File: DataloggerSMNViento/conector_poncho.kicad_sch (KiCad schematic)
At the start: 1 part

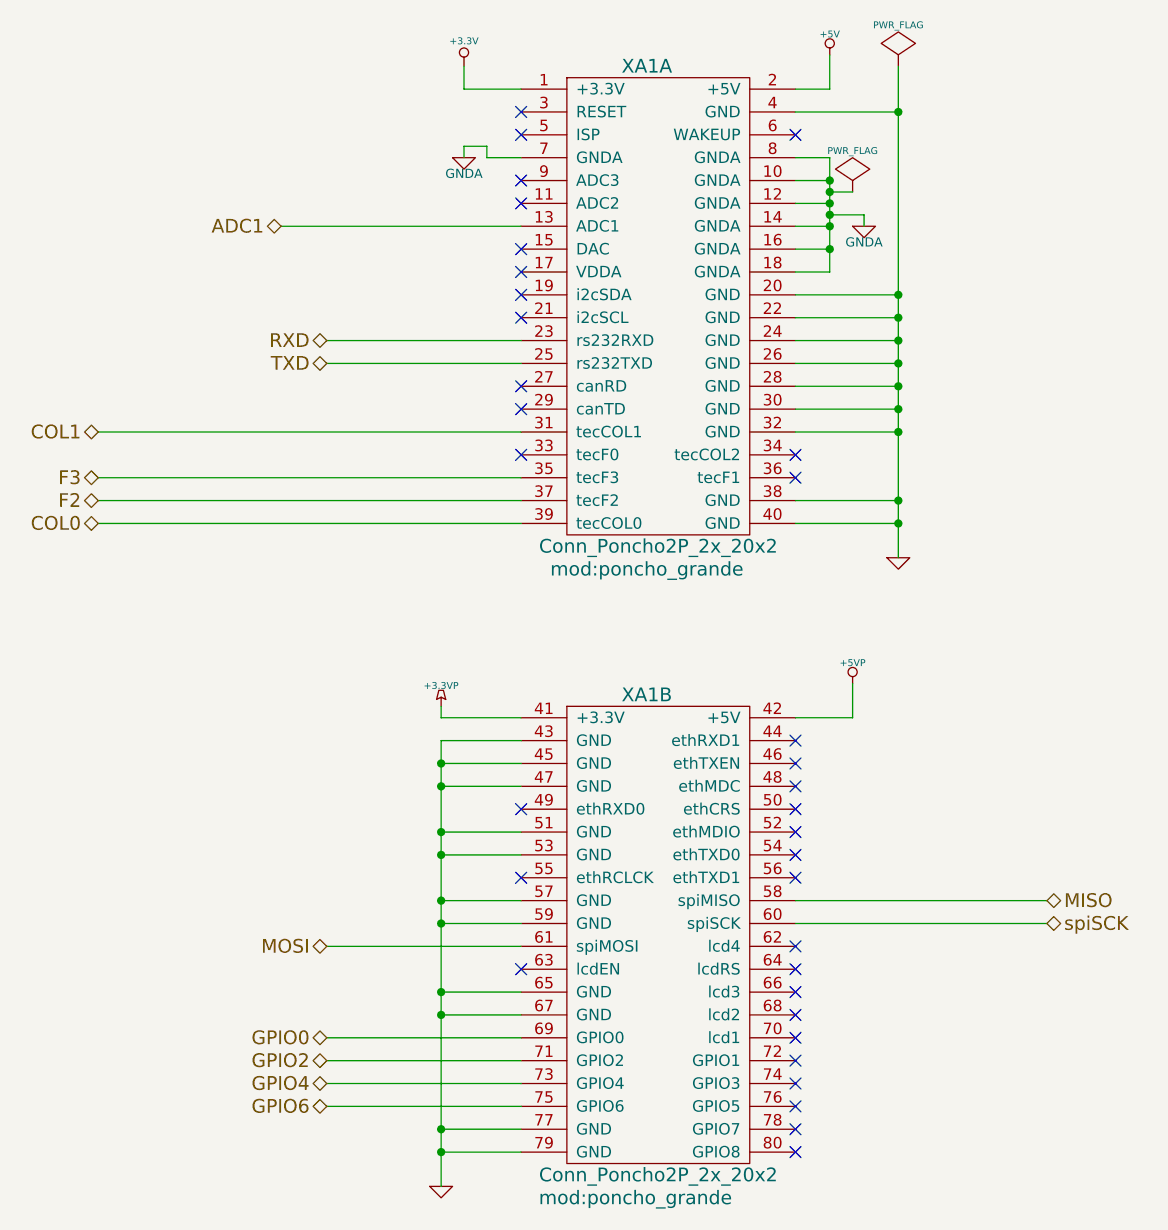
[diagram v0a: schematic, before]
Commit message: Agrego modificaciones al poncho de la EDU CIAA, también agrego una simulacion del circuito para tomar la tensión del ADC del tunnel
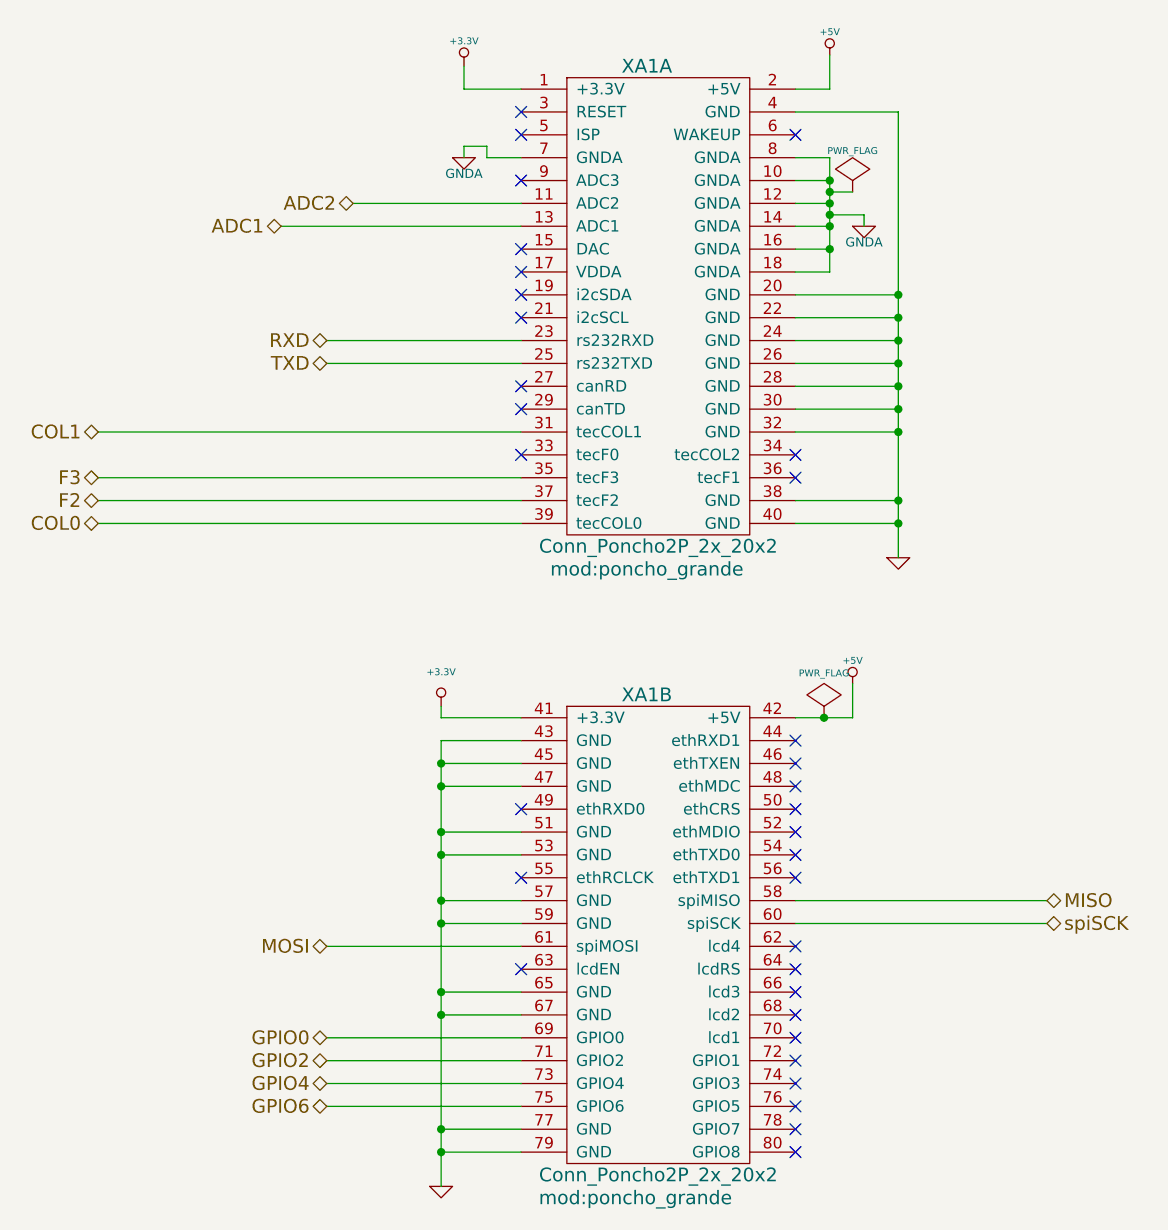
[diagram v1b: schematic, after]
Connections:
- net +3.3VP is gone; now on net +3.3V: XA1.41 (+3.3V)
- net +5VP is gone; now on net +5V: XA1.42 (+5V)
- net ADC2: now reaches XA1.11 (ADC2)
- no-connect marks 34 -> 33
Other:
- company: Compañia: Servicio Meteorologico Nacional - Universidad de Buenos Aires -> Servicio Meteorológico Nacional - FIUBA - UBA
- title: Poncho Grande - Datalogger SMN Viento -> Datalogger para SCTV
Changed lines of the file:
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@@
   (paper "A4")
   (title_block
-    (title "Poncho Grande - Datalogger SMN Viento")
-    (date "2015-10-06")
+    (title "Datalogger para SCTV")
+    (date "2023-10-20")
     (rev "1.0")
-    (company "Compañia: Servicio Meteorologico Nacional - Universidad de Buenos Aires")
-    (comment 1 "https://github.com/ciaa/Ponchos/tree/master/modelos/doc")
-    (comment 2 "Licencia: Ver Licencia.txt UBA")
-    (comment 3 "Autor del poncho: Cristian Zozimo Aranda Cordero. Ver directorio \"doc\"")
-    (comment 4 "CÓDIGO PONCHO:")
+    (company "Servicio Meteorológico Nacional - FIUBA - UBA")
+    (comment 1 "poner repo")
+    (comment 2 "Autores y Licencia del poncho: Cristian Aranda (FIUBA), ver archivo licence.txt")
+    (comment 3 "Autor del poncho: Cristian Zozimo Aranda Cordero.  Ver directorio \"doc\"")
+    (comment 4 "CÓDIGO PONCHO: DT1")
   )
   (junction (at 171.45 66.04) (diameter 0) (color 0 0 0 0)
@@
   (junction (at 171.45 55.88) (diameter 0) (color 0 0 0 0)
   )
-  (junction (at 171.45 33.02) (diameter 0) (color 0 0 0 0)
-  )
   (junction (at 163.83 45.72) (diameter 0) (color 0 0 0 0)
   )
@@
   )
   (junction (at 120.65 133.35) (diameter 0) (color 0 0 0 0)
+  )
+  (junction (at 163.195 100.33) (diameter 0) (color 0 0 0 0)
   )
   (junction (at 120.65 123.19) (diameter 0) (color 0 0 0 0)
@@
   (no_connect (at 160.02 138.43))
   (no_connect (at 160.02 110.49))
-  (no_connect (at 129.54 43.18))
   (no_connect (at 129.54 53.34))
   (no_connect (at 160.02 133.35))
@@
     (stroke (width 0) (type default) (color 0 0 0 0))
   )
+  (wire (pts (xy 163.195 100.33) (xy 160.02 100.33))
+    (stroke (width 0) (type default) (color 0 0 0 0))
+  )
   (wire (pts (xy 163.83 48.26) (xy 163.83 50.8))
     (stroke (width 0) (type default) (color 0 0 0 0))
@@
     (stroke (width 0) (type default) (color 0 0 0 0))
   )
+  (wire (pts (xy 110.871 43.18) (xy 129.54 43.18))
+    (stroke (width 0) (type default) (color 0 0 0 0))
+  )
   (wire (pts (xy 160.02 78.74) (xy 171.45 78.74))
     (stroke (width 0) (type default) (color 0 0 0 0))
@@
     (stroke (width 0) (type default) (color 0 0 0 0))
   )
-  (wire (pts (xy 171.45 27.94) (xy 171.45 33.02))
-    (stroke (width 0) (type default) (color 0 0 0 0))
-  )
   (wire (pts (xy 171.45 63.5) (xy 171.45 66.04))
     (stroke (width 0) (type default) (color 0 0 0 0))
@@
     (stroke (width 0) (type default) (color 0 0 0 0))
   )
-  (wire (pts (xy 163.83 30.48) (xy 160.02 30.48))
-    (stroke (width 0) (type default) (color 0 0 0 0))
-  )
   (wire (pts (xy 120.65 100.33) (xy 120.65 99.06))
     (stroke (width 0) (type default) (color 0 0 0 0))
@@
     (stroke (width 0) (type default) (color 0 0 0 0))
   )
+  (wire (pts (xy 160.02 30.48) (xy 163.83 30.48))
+    (stroke (width 0) (type default) (color 0 0 0 0))
+  )
   (wire (pts (xy 129.54 78.74) (xy 82.55 78.74))
     (stroke (width 0) (type default) (color 0 0 0 0))
@@
     (stroke (width 0) (type default) (color 0 0 0 0))
   )
-  (wire (pts (xy 166.37 100.33) (xy 160.02 100.33))
+  (wire (pts (xy 166.37 100.33) (xy 163.195 100.33))
     (stroke (width 0) (type default) (color 0 0 0 0))
   )
@@
   (hierarchical_label "MISO" (shape bidirectional) (at 187.96 120.65 0)
     (effects (font (size 1.524 1.524)) (justify left))
+  )
+  (hierarchical_label "ADC2" (shape bidirectional) (at 110.871 43.18 180)
+    (effects (font (size 1.524 1.524)) (justify right))
   )
   (hierarchical_label "ADC1" (shape bidirectional) (at 102.87 45.72 180)
@@
     (pin "1")
   )
-  (symbol (lib_id "Misc_Poncho_Grande:+3.3VP") (at 120.65 99.06 0) (unit 1)
-    (in_bom yes) (on_board yes)
-    (property "Reference" "#PWR02" (id 0) (at 121.92 98.298 0)
-      (effects (font (size 0.508 0.508)) hide)
-    )
-    (property "Value" "+3.3VP" (id 1) (at 120.65 96.774 0)
-      (effects (font (size 0.762 0.762)))
-    )
-    (property "Footprint" "" (id 2) (at 120.65 99.06 0)
-      (effects (font (size 1.524 1.524)))
-    )
-    (property "Datasheet" "" (id 3) (at 120.65 99.06 0)
-      (effects (font (size 1.524 1.524)))
-    )
-    (pin "1")
-  )
   (symbol (lib_id "Misc_Poncho_Grande:GNDA") (at 123.19 38.1 0) (unit 1)
     (in_bom yes) (on_board yes)
@@
     (pin "1")
   )
-  (symbol (lib_id "Misc_Poncho_Grande:PWR_FLAG") (at 171.45 27.94 0) (unit 1)
-    (in_bom yes) (on_board yes)
-    (property "Reference" "#FLG02" (id 0) (at 171.45 25.527 0)
-      (effects (font (size 0.762 0.762)) hide)
-    )
-    (property "Value" "PWR_FLAG" (id 1) (at 171.45 23.368 0)
-      (effects (font (size 0.762 0.762)))
-    )
-    (property "Footprint" "" (id 2) (at 171.45 27.94 0)
-      (effects (font (size 1.524 1.524)))
-    )
-    (property "Datasheet" "" (id 3) (at 171.45 27.94 0)
-      (effects (font (size 1.524 1.524)))
-    )
-    (pin "1")
-  )
   (symbol (lib_id "Misc_Poncho_Grande:PWR_FLAG") (at 166.37 41.91 0) (unit 1)
     (in_bom yes) (on_board yes)
@@
     )
     (property "Datasheet" "" (id 3) (at 166.37 41.91 0)
-      (effects (font (size 1.524 1.524)))
-    )
-    (pin "1")
-  )
-  (symbol (lib_id "Misc_Poncho_Grande:+5V") (at 163.83 26.67 0) (unit 1)
-    (in_bom yes) (on_board yes)
-    (property "Reference" "#PWR06" (id 0) (at 163.83 24.384 0)
-      (effects (font (size 0.508 0.508)) hide)
-    )
-    (property "Value" "+5V" (id 1) (at 163.83 24.384 0)
-      (effects (font (size 0.762 0.762)))
-    )
-    (property "Footprint" "" (id 2) (at 163.83 26.67 0)
-      (effects (font (size 1.524 1.524)))
-    )
-    (property "Datasheet" "" (id 3) (at 163.83 26.67 0)
       (effects (font (size 1.524 1.524)))
     )
@@
     (pin "80")
   )
-  (symbol (lib_id "Poncho_Esqueleto:Conn_Poncho2P_2x_20x2") (at 135.89 38.1 0) (unit 1)
+  (symbol (lib_name "Conn_Poncho2P_2x_20x2_1") (lib_id "Poncho_Esqueleto:Conn_Poncho2P_2x_20x2") (at 135.89 38.1 0) (unit 1)
     (in_bom yes) (on_board yes)
     (property "Reference" "XA1" (id 0) (at 143.51 27.94 0)
@@
     (pin "80")
   )
-  (symbol (lib_id "Misc_Poncho_Grande:+5VP") (at 166.37 96.52 0) (unit 1)
-    (in_bom yes) (on_board yes)
-    (property "Reference" "#PWR07" (id 0) (at 166.37 94.234 0)
+  (symbol (lib_id "Misc_Poncho_Grande:+3.3V") (at 120.65 99.06 0) (unit 1)
+    (in_bom yes) (on_board yes) (fields_autoplaced)
+    (property "Reference" "#PWR0104" (id 0) (at 120.65 100.076 0)
+      (effects (font (size 0.762 0.762)) hide)
+    )
+    (property "Value" "+3.3V" (id 1) (at 120.65 95.25 0)
+      (effects (font (size 0.762 0.762)))
+    )
+    (property "Footprint" "" (id 2) (at 120.65 99.06 0)
+      (effects (font (size 1.524 1.524)))
+    )
+    (property "Datasheet" "" (id 3) (at 120.65 99.06 0)
+      (effects (font (size 1.524 1.524)))
+    )
+    (pin "1")
+  )
+  (symbol (lib_id "Misc_Poncho_Grande:+5V") (at 163.83 26.67 0) (unit 1)
+    (in_bom yes) (on_board yes) (fields_autoplaced)
+    (property "Reference" "#PWR0101" (id 0) (at 163.83 24.384 0)
       (effects (font (size 0.508 0.508)) hide)
     )
-    (property "Value" "+5VP" (id 1) (at 166.37 94.234 0)
+    (property "Value" "+5V" (id 1) (at 163.83 24.13 0)
       (effects (font (size 0.762 0.762)))
     )
+    (property "Footprint" "" (id 2) (at 163.83 26.67 0)
+      (effects (font (size 1.524 1.524)))
+    )
+    (property "Datasheet" "" (id 3) (at 163.83 26.67 0)
+      (effects (font (size 1.524 1.524)))
+    )
+    (pin "1")
+  )
+  (symbol (lib_id "Misc_Poncho_Grande:PWR_FLAG") (at 163.195 100.33 0) (unit 1)
+    (in_bom yes) (on_board yes) (fields_autoplaced)
+    (property "Reference" "#FLG0102" (id 0) (at 163.195 97.917 0)
+      (effects (font (size 0.762 0.762)) hide)
+    )
+    (property "Value" "PWR_FLAG" (id 1) (at 163.195 95.377 0)
+      (effects (font (size 0.762 0.762)))
+    )
+    (property "Footprint" "" (id 2) (at 163.195 100.33 0)
+      (effects (font (size 1.524 1.524)))
+    )
+    (property "Datasheet" "" (id 3) (at 163.195 100.33 0)
+      (effects (font (size 1.524 1.524)))
+    )
+    (pin "1")
+  )
+  (symbol (lib_id "Misc_Poncho_Grande:+5V") (at 166.37 96.52 0) (unit 1)
+    (in_bom yes) (on_board yes) (fields_autoplaced)
+    (property "Reference" "#PWR0105" (id 0) (at 166.37 94.234 0)
+      (effects (font (size 0.508 0.508)) hide)
+    )
+    (property "Value" "+5V" (id 1) (at 166.37 93.98 0)
+      (effects (font (size 0.762 0.762)))
+    )

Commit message: Subo la version v1.0 del PCB del poncho de la tesis
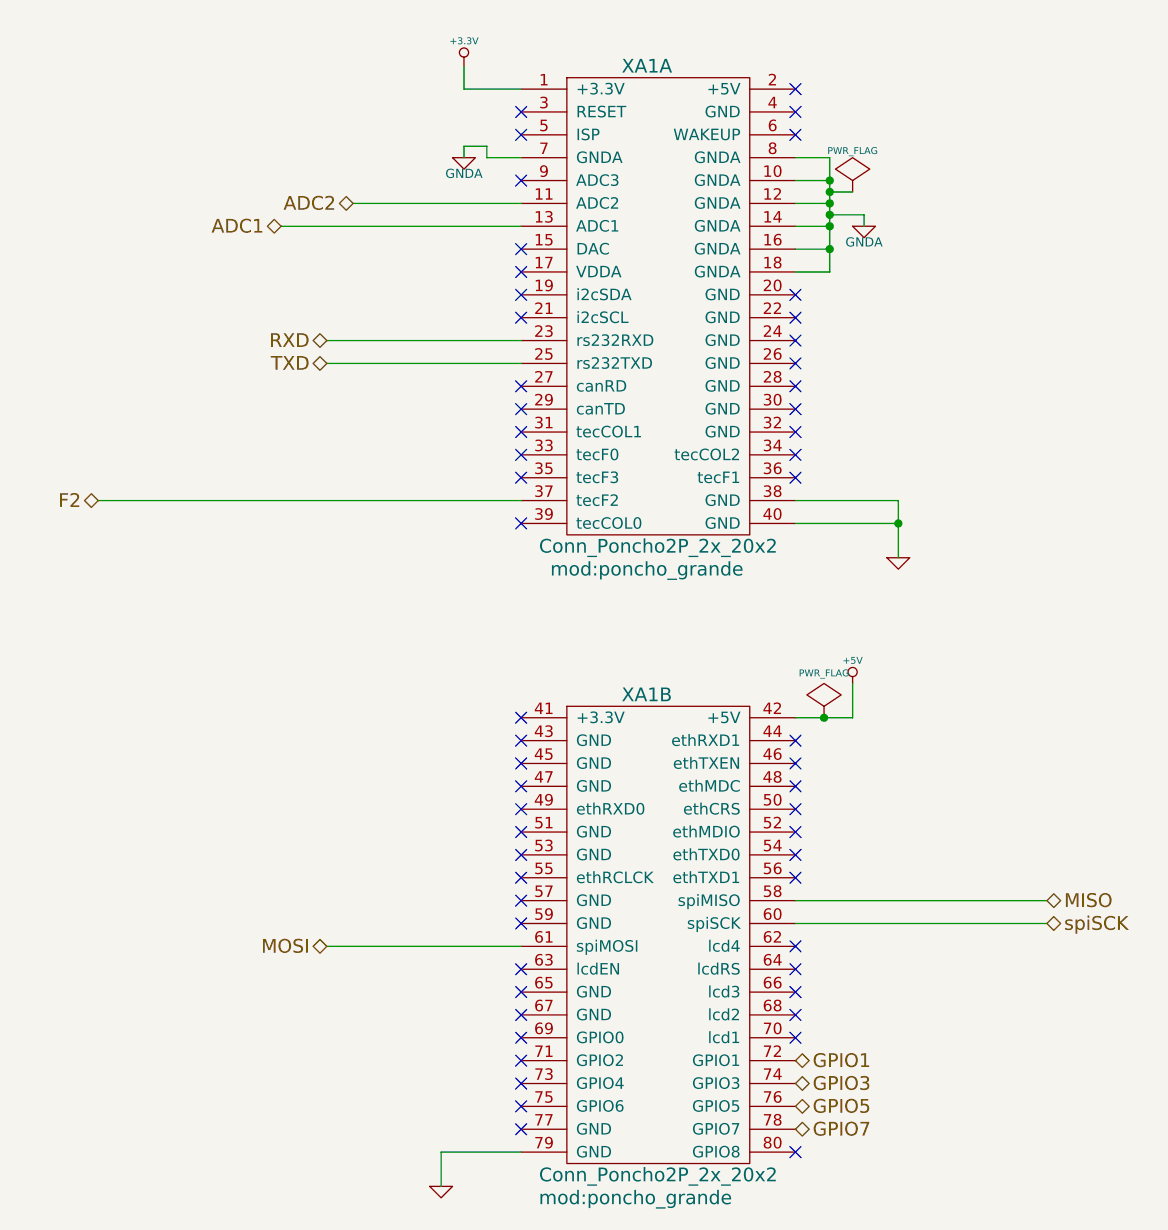
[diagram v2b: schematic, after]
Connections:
- net +3.3V: no longer XA1.41 (+3.3V)
- net +5V: no longer XA1.2 (+5V)
- net GND: no longer XA1.20 (GND), XA1.22 (GND), XA1.24 (GND), XA1.26 (GND), XA1.28 (GND), XA1.30 (GND), XA1.32 (GND), XA1.4 (GND), XA1.43 (GND), XA1.45 (GND), XA1.47 (GND), XA1.51 (GND), XA1.53 (GND), XA1.57 (GND), XA1.59 (GND), XA1.65 (GND), XA1.67 (GND), XA1.77 (GND)
- net GPIO1: now reaches XA1.72 (GPIO1)
- net GPIO3: now reaches XA1.74 (GPIO3)
- net GPIO5: now reaches XA1.76 (GPIO5)
- net GPIO7: now reaches XA1.78 (GPIO7)
- net COL0: no longer names the net of XA1.39 (tecCOL0)
- net COL1: no longer names the net of XA1.31 (tecCOL1)
- net F3: no longer names the net of XA1.35 (tecF3)
- net GPIO0: no longer names the net of XA1.69 (GPIO0)
- net GPIO2: no longer names the net of XA1.71 (GPIO2)
- net GPIO4: no longer names the net of XA1.73 (GPIO4)
- net GPIO6: no longer names the net of XA1.75 (GPIO6)
- no-connect marks 33 -> 56

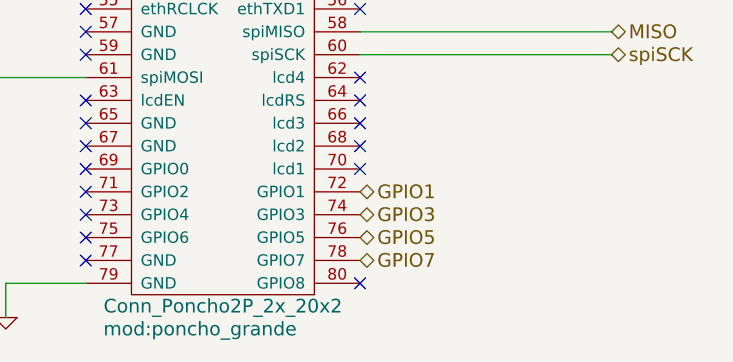
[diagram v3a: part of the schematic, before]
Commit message: Subo la version v1.2 THT de la poncho, para fabricar en el SMN
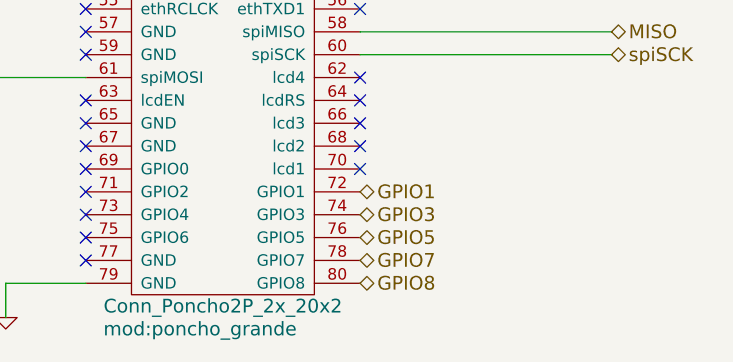
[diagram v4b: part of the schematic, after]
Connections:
- net GPIO8: now reaches XA1.80 (GPIO8)
- no-connect marks 56 -> 55
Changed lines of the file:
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@@
   (no_connect (at 129.54 63.5))
   (no_connect (at 160.02 130.81))
-  (no_connect (at 160.02 148.59))
   (no_connect (at 129.54 115.57))
   (no_connect (at 129.54 100.33))
@@
     (effects (font (size 1.524 1.524)) (justify left))
   )
+  (hierarchical_label "GPIO8" (shape bidirectional) (at 160.02 148.59 0)
+    (effects (font (size 1.524 1.524)) (justify left))
+  )
